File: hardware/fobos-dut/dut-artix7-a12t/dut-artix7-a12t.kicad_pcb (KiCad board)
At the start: 2 copper layers, 140 parts, among them J1 Target, J3 1050753001, J4 Glitch, J5 Conn_01x02, J6 Measure, J7 0878321420, J8 1050752001, Q1 FDS9435A, Q2 MBT3904DW1, Q3 FDV301N, SW1 SW_DIP_x03, U1 XC7A12T-CSG325, U2 SP3003-04ATG, U3 SP3003-04ATG, U4 SP3003-04ATG, U5 INA225, U6 BGA2801, U7 TS3A27518EIPWRQ1, U8 LTC3569EFE#PBF, U9 IS25LP256D-JMLE

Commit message: Schematic is 99% complete, getting started on layout
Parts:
- added D2: LG_L29K-G2J1-24-Z, digikey-footprints:0603, F.Cu at (285.9, 32.6)
- added D3: LG_L29K-G2J1-24-Z, digikey-footprints:0603, F.Cu at (277.2, 40.0)
- added D4: LG_L29K-G2J1-24-Z, digikey-footprints:0603, F.Cu at (281.2, 37.6)
- added H1: MountingHole, cerg:MH_4-40, F.Cu at (5.08, 71.1)
- added H2: MountingHole, cerg:MH_4-40, F.Cu at (5.08, 5.08)
- added H3: MountingHole, cerg:MH_4-40, F.Cu at (83.8, 71.1)
- added H4: MountingHole, cerg:MH_4-40, F.Cu at (83.8, 5.08)
- added J2: Pmod 2x6, Connector_PinHeader_2.54mm:PinHeader_2x06_P2.54mm_Horizontal, F.Cu at (6.35, 62.2)
- added L3: 1.5uH, cerg:L_SRN2012, B.Cu at (129.2, 41.1)
- added L4: 3.3uH, cerg:L_BRC2012, B.Cu at (129.2, 37.9)
- added L5: 2.2uH, cerg:L_SRN2012, B.Cu at (133.1, 41.1)
- added Q4: FDV301N, digikey-footprints:SOT-23-3, F.Cu at (273.1, 33.8)
- added Q5: FDV301N, digikey-footprints:SOT-23-3, F.Cu at (273.1, 38.8)
- added Q6: FDV301N, digikey-footprints:SOT-23-3, F.Cu at (277.8, 33.8)
- added R52: 4.7KR, Resistor_SMD:R_0603_1608Metric, F.Cu at (341.5, 53.3)
- added R53: 330R, Resistor_SMD:R_0603_1608Metric, F.Cu at (354.3, 50.8)
- added R54: 4.7KR, Resistor_SMD:R_0603_1608Metric, F.Cu at (354.3, 53.3)
- added R55: 4.7KR, Resistor_SMD:R_0603_1608Metric, F.Cu at (358.3, 50.8)
- added R56: 33R, Resistor_SMD:R_0603_1608Metric, F.Cu at (345.5, 50.8)
- added R57: 800R, Resistor_SMD:R_0603_1608Metric, F.Cu at (282.1, 32.6)
- added R58: 800R, Resistor_SMD:R_0603_1608Metric, F.Cu at (277.4, 37.6)
- added R59: 800R, Resistor_SMD:R_0603_1608Metric, F.Cu at (282.1, 35.1)
- added R60: 10KR, Resistor_SMD:R_0603_1608Metric, F.Cu at (168.9, 137.2)
- added R61: 10KR, Resistor_SMD:R_0603_1608Metric, F.Cu at (172.9, 137.2)
- added R62: 10KR, Resistor_SMD:R_0603_1608Metric, F.Cu at (168.9, 139.7)
- added R63: 10KR, Resistor_SMD:R_0603_1608Metric, F.Cu at (189.4, 128.9)
- added R64: 10KR, Resistor_SMD:R_0603_1608Metric, F.Cu at (172.9, 139.7)
- added R65: 10KR, Resistor_SMD:R_0603_1608Metric, F.Cu at (176.9, 137.2)
- added R66: 10KR, Resistor_SMD:R_0603_1608Metric, F.Cu at (189.4, 131.4)
- added S2: 1825910-6, digikey-footprints:Switch_Tactile_THT_6x6mm, F.Cu at (71.1, 72.5)
- added S4: 1825910-6, digikey-footprints:Switch_Tactile_THT_6x6mm, F.Cu at (50.8, 72.5)
- added S5: 1825910-6, digikey-footprints:Switch_Tactile_THT_6x6mm, F.Cu at (61.0, 72.5)
- C17, C18, C19, C20, C21, C22, C23, C25, C29, C30, C32, C34, C35, Q2, R34, R35, R36, R37, R38, R39, R40, R41, R42, R43, R44, R45, R46, R47, R48, U8: moved to B.Cu
- J3: value 1050753001 -> 575-8; footprint cerg:105075X001 -> cerg:575-8
- J8: value 1050752001 -> 575-8; footprint cerg:105075X001 -> cerg:575-8
- R25: value 4K7 -> 4.7KR
- R26: value 33R -> 4.7KR
- R29, R30: value 1R -> 0R
- R31, R32, R33: value 4k7 -> 4.7KR
- moved TP1 440.4 mm to (316.2, 87.6)
- moved TP7 425.6 mm to (312.4, 87.6)
- moved R26 417.7 mm to (341.5, 50.8)
- moved TP5 415.1 mm to (308.6, 87.6)
- moved TP6 408.2 mm to (304.8, 87.6)
- moved C2 406.3 mm to (256.4, 72.7)
- moved C3 406.3 mm to (256.4, 65.2)
- moved R15 406.3 mm to (256.4, 70.2)
- moved R18 406.3 mm to (256.4, 67.7)
- moved R5 406.3 mm to (256.4, 77.7)
- moved R9 406.3 mm to (256.4, 75.2)
- moved C1 406.3 mm to (260.4, 65.2)
- moved C10 406.3 mm to (252.7, 123.3)
- moved C26 406.3 mm to (345.9, 66.7)
- moved C27 406.3 mm to (345.9, 70.9)
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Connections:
- C16 pad 1: +1V0 -> +3V3
- C19 pad 1: +1V0 -> +1V8
- C20 pad 1: +1V0 -> +3V3
- C22 pad 1: +1V0 -> +1V8
- C23 pad 1: +1V0 -> +3V3
- C25 pad 1: +1V0 -> VCC
- C26 pad 1: +1V0 -> +1V8
- C27 pad 1: +1V0 -> +3V3
- C28 pad 1: +1V0 -> +1V8
- C29 pad 1: +1V0 -> VCC
- C30 pad 1: +1V0 -> VCC
- C31 pad 1: +1V0 -> +1V8
- C32 pad 1: +1V0 -> VCC
- C33 pad 1: +1V0 -> +1V8
- C34 pad 1: +1V0 -> VCC
- C35 pad 1: +1V0 -> VCC
- C36 pad 1: +1V0 -> +3V3
- C37 pad 1: +1V0 -> +3V3
- C38 pad 1: +1V0 -> +3V3
- C39 pad 1: +1V0 -> +3V3
- C40 pad 1: +1V0 -> +3V3
- C41 pad 1: +1V0 -> +3V3
- C42 pad 1: +1V0 -> +3V3
- C43 pad 1: +1V0 -> +3V3
- C44 pad 1: +1V0 -> +3V3
- C45 pad 1: +1V0 -> +3V3
- C46 pad 1: +1V0 -> +3V3
- C47 pad 1: +1V0 -> +3V3
- C48 pad 1: +1V0 -> +3V3
- C49 pad 1: +1V0 -> +3V3
- C50 pad 1: +1V0 -> +3V3
- C51 pad 1: +1V0 -> +3V3
- C52 pad 1: +1V0 -> +3V3
- C53 pad 1: +1V0 -> +3V3
- J4 pad 1: +1V0 -> VCC
- J5 pad 1: +1V0 -> VCC
- J7 pad 2: +1V0 -> +3V3
- JP3 pad 2: +1V0 -> VCC
- R23 pad 1: +1V0 -> VCC
- R24 pad 2: +1V0 -> VCC
- R25 pad 2: +1V0 -> +3V3
- R26 pad 2: /FPGA 1/FPGA_CCLK -> +3V3
- R29 pad 1: Net-(R29-Pad1) -> SW_CLK
- R29 pad 2: /FPGA 1/FPGA_CCLK -> Net-(R29-Pad2)
- R30 pad 1: Net-(R30-Pad1) -> SW_DIN
- R31 pad 1: +1V0 -> +3V3
- R32 pad 1: +1V0 -> +3V3
- R33 pad 1: +1V0 -> +3V3
- R34 pad 2: +1V0 -> +1V8
- R44 pad 2: +1V0 -> +1V8
- R45 pad 2: +1V0 -> +3V3
- TP6 pad 1: +1V0 -> +1V8
- TP7 pad 1: +1V0 -> +3V3
- U1 pad A16: +1V0 -> +3V3
- U1 pad B13: +1V0 -> +3V3
- U1 pad C10: +1V0 -> +3V3
- U1 pad D17: +1V0 -> +3V3
- U1 pad E10: +1V0 -> +3V3
- U1 pad E12: +1V0 -> VCC
- U1 pad E14: +1V0 -> +3V3
- U1 pad E8: /FPGA 1/FPGA_CCLK -> Net-(R29-Pad2)
- U1 pad F11: +1V0 -> VCC
- U1 pad F12: Net-(U1-PadF12) -> SW_DONE
- U1 pad F7: +1V0 -> VCC
- U1 pad F9: +1V0 -> VCC
- U1 pad G10: +1V0 -> VCC
- U1 pad G12: +1V0 -> +1V8
- U1 pad G18: +1V0 -> +3V3
- U1 pad G8: +1V0 -> VCC
- U1 pad H11: +1V0 -> VCC
- U1 pad H13: +1V0 -> +1V8
- U1 pad H15: +1V0 -> +3V3
- U1 pad H7: +1V0 -> VCC
- U1 pad H9: +1V0 -> VCC
- U1 pad J10: +1V0 -> +1V8
- U1 pad J12: +1V0 -> VCC
- U1 pad J8: +1V0 -> VCC
- U1 pad K11: +1V0 -> VCC
- U1 pad K13: +1V0 -> +1V8
- U1 pad K7: +1V0 -> VCC
- U1 pad L12: +1V0 -> VCC
- U1 pad L15: Net-(R25-Pad1) -> Net-(R26-Pad1)
- U1 pad L16: +1V0 -> +3V3
- U1 pad L6: +1V0 -> +3V3
- U1 pad L8: +1V0 -> VCC
- U1 pad M11: +1V0 -> VCC
- U1 pad M13: +1V0 -> +1V8
- U1 pad M3: +1V0 -> +3V3
- U1 pad M7: +1V0 -> VCC
- U1 pad N10: +1V0 -> VCC
- U1 pad N12: +1V0 -> VCC
- U1 pad N8: +1V0 -> VCC
- U1 pad P10: Net-(U1-PadP10) -> SW_PROGRAM_B
- U1 pad P11: +1V0 -> VCC
- U1 pad P13: +1V0 -> +1V8
- U1 pad P17: +1V0 -> +3V3
- U1 pad P7: +1V0 -> +3V3
- U1 pad P9: +1V0 -> VCC
- U1 pad R10: +1V0 -> +3V3
- U1 pad R14: +1V0 -> +3V3
- U1 pad R4: +1V0 -> +3V3
- U1 pad T1: +1V0 -> +3V3
- U1 pad T10: Net-(U1-PadT10) -> SW_INIT_B
- U1 pad T11: +1V0 -> +3V3
- U1 pad U18: +1V0 -> +3V3
- U1 pad U8: +1V0 -> +3V3
- U1 pad V15: +1V0 -> +3V3
- U1 pad V5: +1V0 -> +3V3
- U5 pad 8: +1V0 -> VCC
- U9 pad 10: Net-(U9-Pad10) -> GND
- U9 pad 15: Net-(U9-Pad15) -> Net-(R27-Pad2)
- U9 pad 2: Net-(U9-Pad2) -> +3V3
- U9 pad 7: Net-(U9-Pad7) -> Net-(R26-Pad1)
- U9 pad 8: Net-(U9-Pad8) -> Net-(R28-Pad2)
- U9 pad 9: Net-(U9-Pad9) -> Net-(R25-Pad1)
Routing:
- net GND: track 0.00 -> 53.3 mm, vias 0 -> 94
- net +3V3: track 0.00 -> 13.6 mm, vias 0 -> 22
- net VCC: track 0.00 -> 11.9 mm, vias 0 -> 21
- net +1V8: track 0.00 -> 3.39 mm, vias 0 -> 6
- net SW_INIT_B: track 0.00 -> 0.57 mm, vias 0 -> 1
- net SW_PROGRAM_B: track 0.00 -> 0.57 mm, vias 0 -> 1
- net Net-(R29-Pad2): track 0.00 -> 0.57 mm, vias 0 -> 1
- added copper zone on In1.Cu, net GND
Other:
- board outline added: 88.9 x 76.2 mm
- copper layers 2 -> 4
- rule trace_min: 0.2 -> 0.127
- rule via_min_drill: 0.3 -> 0.254
- rule via_min_size: 0.4 -> 0.254

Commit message: Preliminary placement underway Made a copy of cerg 3d model within Artix 7 dut project to resolve nagging library path issue
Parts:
- added D5: LG_L29K-G2J1-24-Z, digikey-footprints:0603, F.Cu at (133.3, 67.3)
- added J9: Measure, cerg:SMA-JOHNSON-142-0701-801, F.Cu at (48.3, 2.54)
- added Q7: BSS138, Package_TO_SOT_SMD:SOT-23, F.Cu at (129.3, 68.3)
- added R67: 0R, Resistor_SMD:R_0603_1608Metric, F.Cu at (12.4, 49.0)
- added R68: 10KR, Resistor_SMD:R_0603_1608Metric, F.Cu at (124.4, 72.3)
- added R69: 470R, Resistor_SMD:R_0603_1608Metric, F.Cu at (129.1, 71.9)
- added R70: 10KR, Resistor_SMD:R_0603_1608Metric, F.Cu at (173.6, 94.5)
- added R71: 10KR, Resistor_SMD:R_0603_1608Metric, F.Cu at (177.6, 95.2)
- added SW2: SW_DIP_x03, cerg:DS04-254-2-03BK-SMT, F.Cu at (185.2, 87.9)
- C26, C27: footprint Resistor_SMD:R_1210_3225Metric_Pad1.30x2.65mm_HandSolder -> Resistor_SMD:R_0805_2012Metric_Pad1.20x1.40mm_HandSolder; moved to B.Cu
- C28, C39: footprint Resistor_SMD:R_0805_2012Metric_Pad1.20x1.40mm_HandSolder -> Resistor_SMD:R_0402_1005Metric_Pad0.72x0.64mm_HandSolder; moved to B.Cu
- C29, C37, C40, C41: footprint Resistor_SMD:R_0805_2012Metric_Pad1.20x1.40mm_HandSolder -> Resistor_SMD:R_0402_1005Metric_Pad0.72x0.64mm_HandSolder
- C30, C32, C34: footprint Resistor_SMD:R_0603_1608Metric_Pad0.98x0.95mm_HandSolder -> Resistor_SMD:R_0402_1005Metric_Pad0.72x0.64mm_HandSolder
- C31, C33, C42, C43, C44, C45, C46, C47, C48, C49, C50, C51, C52, C53: footprint Resistor_SMD:R_0603_1608Metric_Pad0.98x0.95mm_HandSolder -> Resistor_SMD:R_0402_1005Metric_Pad0.72x0.64mm_HandSolder; moved to B.Cu
- C35: footprint Resistor_SMD:R_1210_3225Metric_Pad1.30x2.65mm_HandSolder -> Resistor_SMD:R_0805_2012Metric_Pad1.20x1.40mm_HandSolder
- C36, R7, R9, U2, U3, U4: moved to B.Cu
- R57, R58, R59: value 800R -> 470R
- U7: value TS3A27518EIPWRQ1 -> TS3A5018DBQR; footprint Package_SO:TSSOP-24_4.4x7.8mm_P0.65mm -> cerg:SSOP-16_4.0x5.0mm_P0.635mm
- moved C44 331.9 mm to (39.4, 109.6)
- moved C49 327.1 mm to (44.2, 31.8), turned to 90 degrees
- moved C43 319.9 mm to (50.8, 29.7)
- moved C47 319.7 mm to (50.8, 42.9), turned to 180 degrees
- moved C46 319.2 mm to (45.9, 113.6)
- moved C45 319.2 mm to (47.5, 30.2), turned to 90 degrees
- moved C51 318.0 mm to (43.7, 44.2), turned to 90 degrees
- moved C48 317.3 mm to (49.0, 44.2), turned to 270 degrees
- moved C31 317.2 mm to (49.3, 37.3)
- moved C33 317.1 mm to (49.3, 40.6)
- moved C52 315.6 mm to (52.6, 33.3)
- moved C41 311.0 mm to (46.4, 102.2)
- moved C42 310.3 mm to (50.8, 38.6)
- moved C28 310.3 mm to (48.5, 34.8)
- moved C50 309.0 mm to (49.1, 113.6)
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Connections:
- net VCC renamed VCCINT
- R59 pad 2: Net-(Q6-Pad3) -> Net-(Q7-Pad3)
- R62 pad 2: Net-(Q6-Pad1) -> Net-(R62-Pad2)
- U7 pad 1: FC_DIO0_MUX -> FC_PROG
- U7 pad 10: FC_DIO3 -> SW_INIT_B
- U7 pad 11: SW_DONE -> FC_DIO3_MUX
- U7 pad 12: Net-(U7-Pad12) -> FC_DIO2
- U7 pad 13: SW_CLK -> SW_PROGRAM_B
- U7 pad 14: FC_PROG -> FC_DIO2_MUX
- U7 pad 15: SW_DIN -> FC_3V3
- U7 pad 16: Net-(U7-Pad16) -> FC_3V3
- U7 pad 2: Net-(U7-Pad2) -> FC_DIO0_MUX
- U7 pad 3: Net-(U7-Pad3) -> SW_CLK
- U7 pad 4: FD_TF -> FC_DIO0
- U7 pad 5: GND -> FC_DIO1_MUX
- U7 pad 6: FC_DIO0 -> SW_DIN
- U7 pad 8: FC_3V3 -> Net-(U7-Pad8)
- U7 pad 9: FC_DIO2 -> FC_DIO3
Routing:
- net GND: track 53.3 -> 89.1 mm, vias 94 -> 103
- net +3V3: track 13.6 -> 33.5 mm, vias 22 -> 25
- net +1V8: track 3.39 -> 10.3 mm, vias 6 -> 8
- net VCCINT: track 11.9 -> 18.8 mm, vias 21 -> 25
- net SW_DONE: track 0.00 -> 0.57 mm, vias 0 -> 1

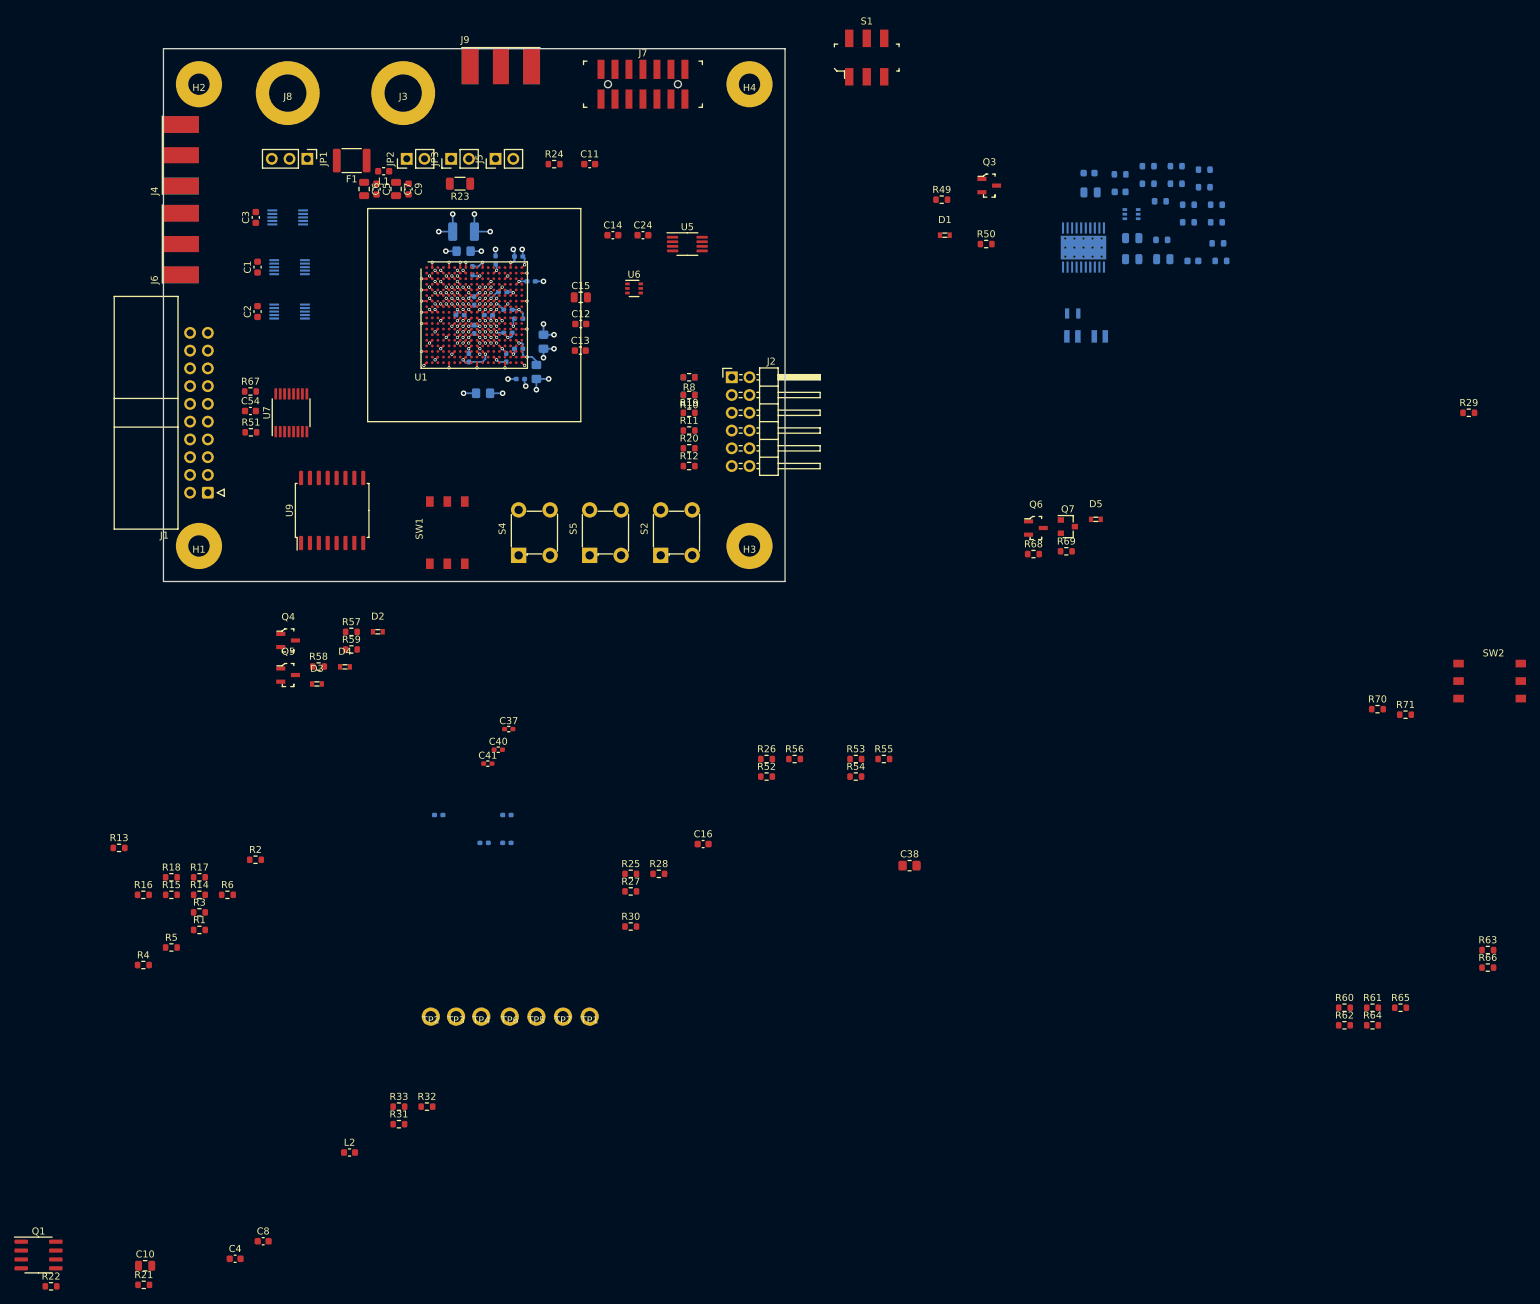
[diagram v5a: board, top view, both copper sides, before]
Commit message: Coarse placement of all components within board outline, began to route traces
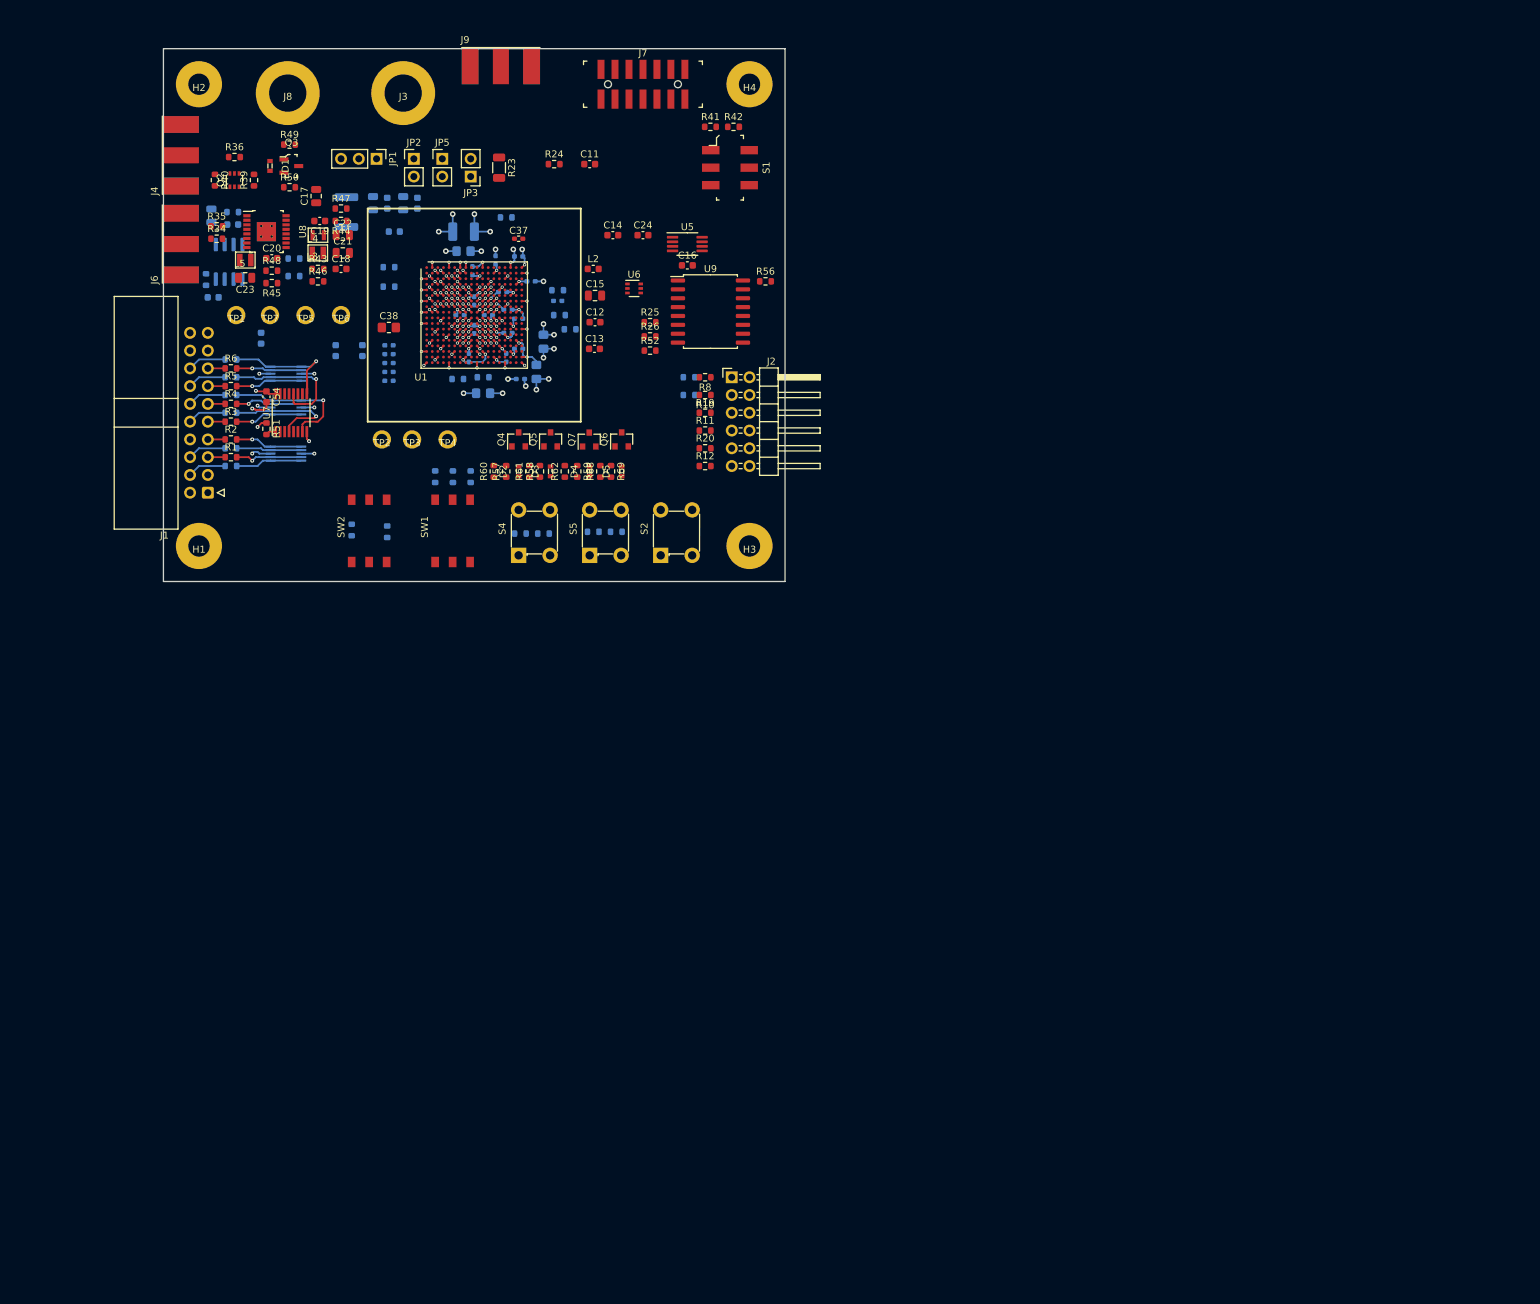
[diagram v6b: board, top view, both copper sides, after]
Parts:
- C1, C10, C2, C3, C4, C40, C41, C5, C6, C7, C8, C9, F1, L1, Q1, R13, R14, R15, R16, R17, R18, R21, R22, R27, R28, R29, R30, R31, R32, R33, R53, R54, R55, R63, R64, R65, R66, R67, R70, R71: moved to B.Cu
- C17, C18, C19, C20, C21, C22, C23, L3, L4, L5, Q2, R34, R35, R36, R39, R40, R41, R42, R43, R44, R45, R46, R47, R48: moved to F.Cu
- Q4, Q5, Q6: value FDV301N -> BSS138; footprint digikey-footprints:SOT-23-3 -> Package_TO_SOT_SMD:SOT-23
- U8: footprint digikey-footprints:TSSOP-20-1EP_W4.4mm -> digikey-footprints:TSSOP-16-1EP_W4.40mm; moved to F.Cu
- moved SW2 159.0 mm to (26.9, 73.4), turned to 90 degrees
- moved R22 155.8 mm to (9.91, 23.4), turned to 180 degrees
- moved R29 155.5 mm to (32.3, 34.0)
- moved C10 150.5 mm to (6.86, 23.9), turned to 90 degrees
- moved R70 148.9 mm to (26.9, 68.8), turned to 270 degrees
- moved R71 148.0 mm to (32.0, 69.1), turned to 270 degrees
- moved R63 147.6 mm to (54.4, 69.3)
- moved C8 145.5 mm to (9.91, 25.1)
- moved Q1 144.6 mm to (9.40, 30.5), turned to 90 degrees
- moved R21 144.1 mm to (6.10, 33.0), turned to 270 degrees
- moved R60 143.8 mm to (47.2, 60.5), turned to 90 degrees
- moved R40 143.4 mm to (7.37, 18.8), turned to 270 degrees
- moved R61 142.9 mm to (52.3, 60.5), turned to 90 degrees
- moved R36 141.2 mm to (10.2, 15.5)
- moved R64 140.7 mm to (51.1, 69.3)
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- renumbered J5 to JP5
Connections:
- R62 pad 2: Net-(R62-Pad2) -> Net-(Q7-Pad1)
- U2 pad 1: (Ready)FC2D_HS -> FD2C_HS
- U2 pad 10: (Ready)FC2D_HS -> FD2C_HS
- U2 pad 4: (Valid)FD2C_HS -> FC_PROG
- U2 pad 7: (Valid)FD2C_HS -> FC_PROG
- U3 pad 1: FC_RST -> FD_TF
- U3 pad 10: FC_RST -> FD_TF
- U3 pad 2: FC_IO -> FC_DIO0
- U3 pad 4: FC_DIO0 -> FC2D_HS
- U3 pad 7: FC_DIO0 -> FC2D_HS
- U3 pad 9: FC_IO -> FC_DIO0
- U4 pad 2: FC2D_CLK -> FC_RST
- U4 pad 4: FD_TF -> FC2D_CLK
- U4 pad 5: (Aux)FC_PROG -> FC_IO
- U4 pad 6: (Aux)FC_PROG -> FC_IO
- U4 pad 7: FD_TF -> FC2D_CLK
- U4 pad 9: FC2D_CLK -> FC_RST
- U7 pad 8: Net-(U7-Pad8) -> GND
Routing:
- net FC_DIO1: track 0.00 -> 19.6 mm, vias 0 -> 1
- net FC_DIO3: track 0.00 -> 19.5 mm, vias 0 -> 1
- net FC_DIO2: track 0.00 -> 19.4 mm, vias 0 -> 1
- net FC_DIO0: track 0.00 -> 17.2 mm, vias 0 -> 1
- net GND: track 89.1 -> 100.8 mm, vias 103 -> 109
- net FC_PROG: track 0.00 -> 10.9 mm, vias 0 -> 1
- net FC_3V3: track 0.00 -> 10.1 mm, vias 0 -> 4
- net FD_TF: track 0.00 -> 9.68 mm, vias 0 -> 1
- net FC_IO: track 0.00 -> 9.68 mm, vias 0 -> 1
- net FC_RST: track 0.00 -> 9.67 mm, vias 0 -> 1
- net FC2D_HS: track 0.00 -> 9.64 mm, vias 0 -> 1
- net FD2C_HS: track 0.00 -> 9.57 mm, vias 0 -> 1
- net FD2C_CLK: track 0.00 -> 9.57 mm
- net FC2D_CLK: track 0.00 -> 9.36 mm
- net /Connectors, IO/CW_TARG1: track 0.00 -> 5.54 mm
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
